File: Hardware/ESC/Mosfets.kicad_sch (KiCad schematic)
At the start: 14 parts, among them Q1 GT011N03TLE, Q2 GT011N03TLE, Q3 GT011N03TLE, Q4 GT011N03TLE, Q5 GT011N03TLE, Q6 GT011N03TLE

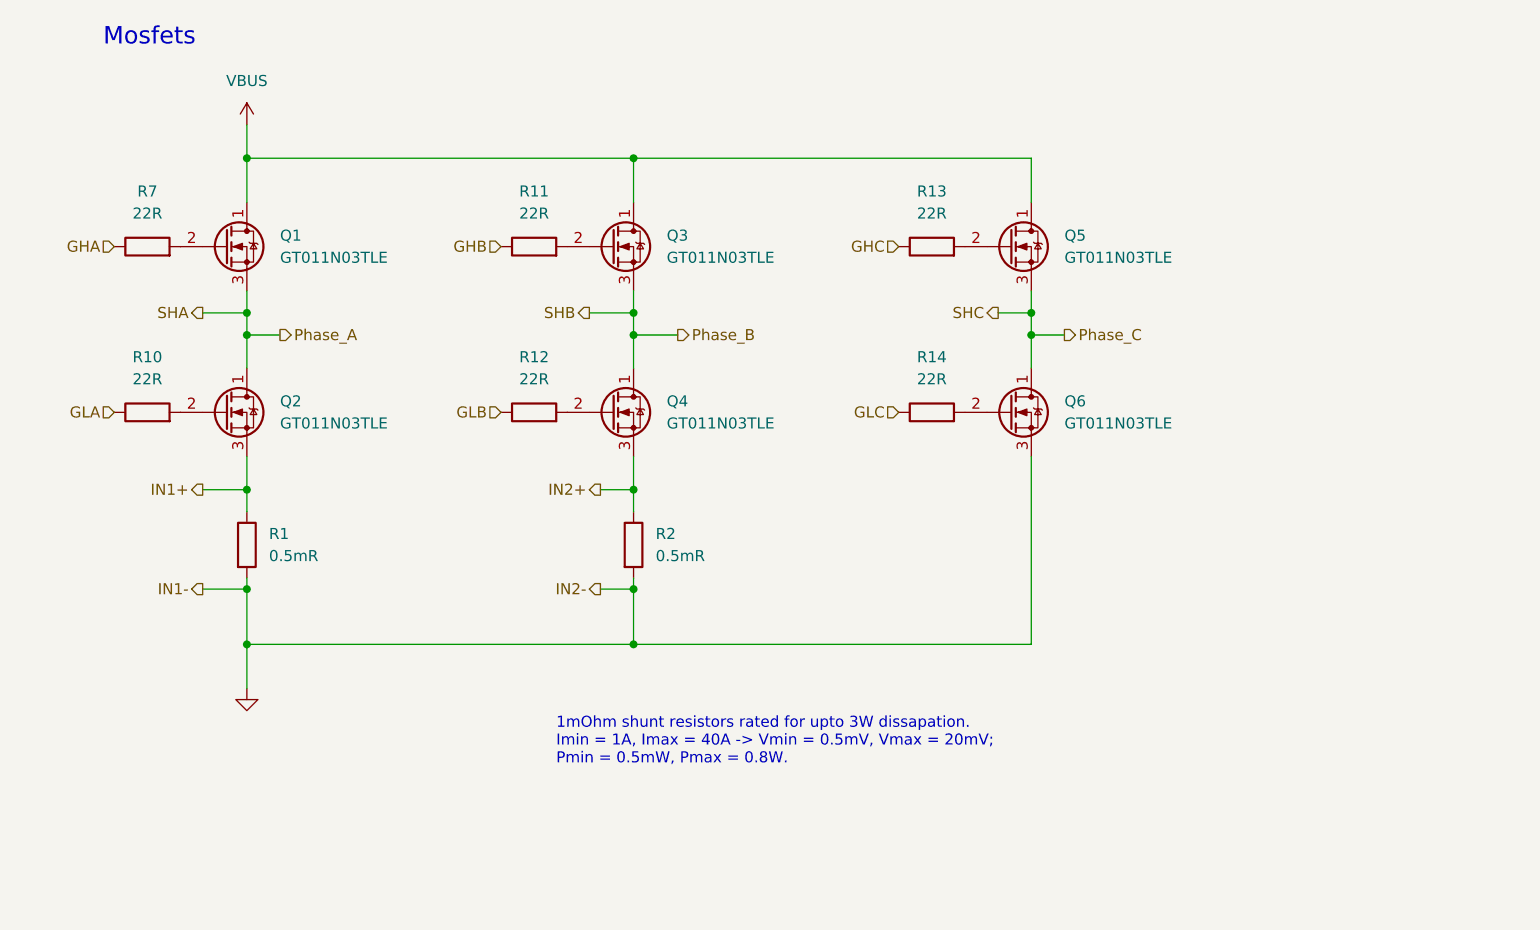
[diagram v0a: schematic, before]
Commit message: Breaking + BEMF ZCD Detector
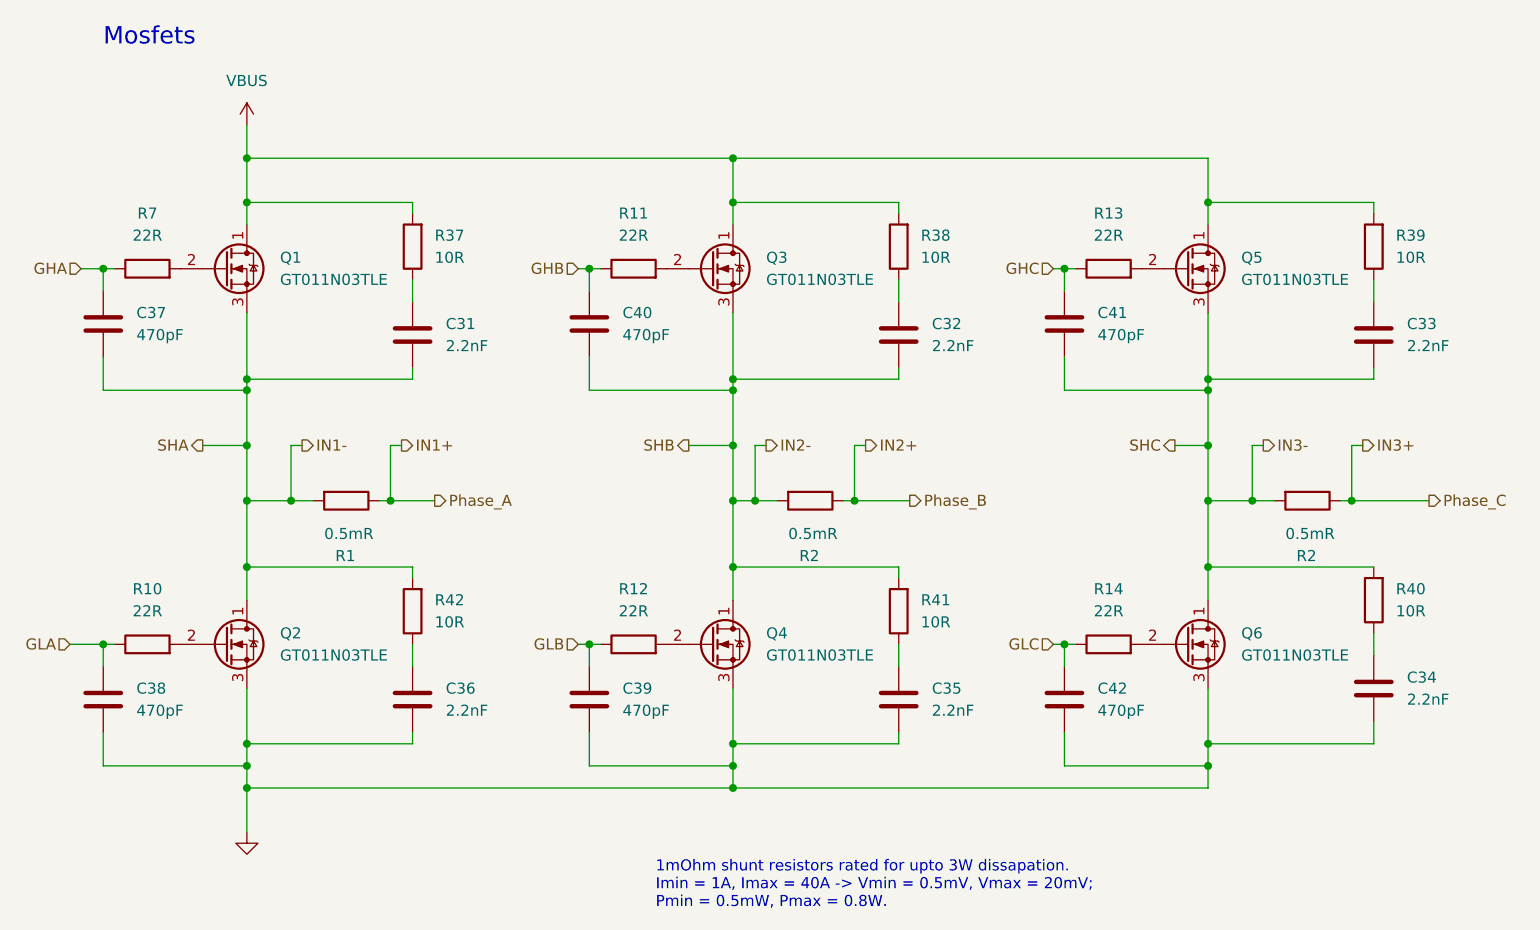
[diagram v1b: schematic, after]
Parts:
- removed R2: 0.5mR, symbol Device:R
- added C31, C32, C33, C34, C35, C36: 2.2nF, symbol Device:C
- added C37, C38, C39, C40, C41, C42: 470pF, symbol Device:C
- added R2 (x2): 0.5mR, symbol Device:R
- added R37, R38, R39, R40, R41, R42: 10R, symbol Device:R
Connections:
- net GHA: now also C37.1
- net GHB: now also C40.1
- net GHC: now also C41.1
- net GLA: now also C38.1
- net GLB: now also C39.1
- net GLC: now also C42.1
- net GND: now also Q2.3 (S), Q4.3 (S), C34.2, C35.2, C36.2, C38.2, C39.2, C42.2; no longer R1.2
- net IN1+: no longer Q2.3 (S)
- net IN2+: now also R2.1; no longer Q4.3 (S)
- net VBUS: now also R37.2, R38.2, R39.2
- net Phase_A renamed IN1-
- net IN1-: now also R1.2, C31.2, C37.2, R42.2
- net Phase_B renamed IN2-
- net IN2-: now also C32.2, C40.2, R2.2, R41.2
- net Phase_C renamed IN3-
- net IN3-: now also C33.2, C41.2, R2.2, R40.2
- new net: C34.1, R40.1
- new net: C31.1, R37.1
- new net: C33.1, R39.1
- new net: C35.1, R41.1
- new net: C32.1, R38.1
- new net: C36.1, R42.1
- new net IN3+: R2.1
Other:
- moved on the sheet: Q1, Q2, Q3, Q4, Q5, Q6, R10, R11, R12, R13, R14, R7
